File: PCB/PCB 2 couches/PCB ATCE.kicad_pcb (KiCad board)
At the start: 2 copper layers, 40.2 x 33.2 mm, 30 parts, among them J1 USB_OTG, J2 Conn_Coaxial, SW1 SW_Push, SW2 SW_Push, Y1 16MHz

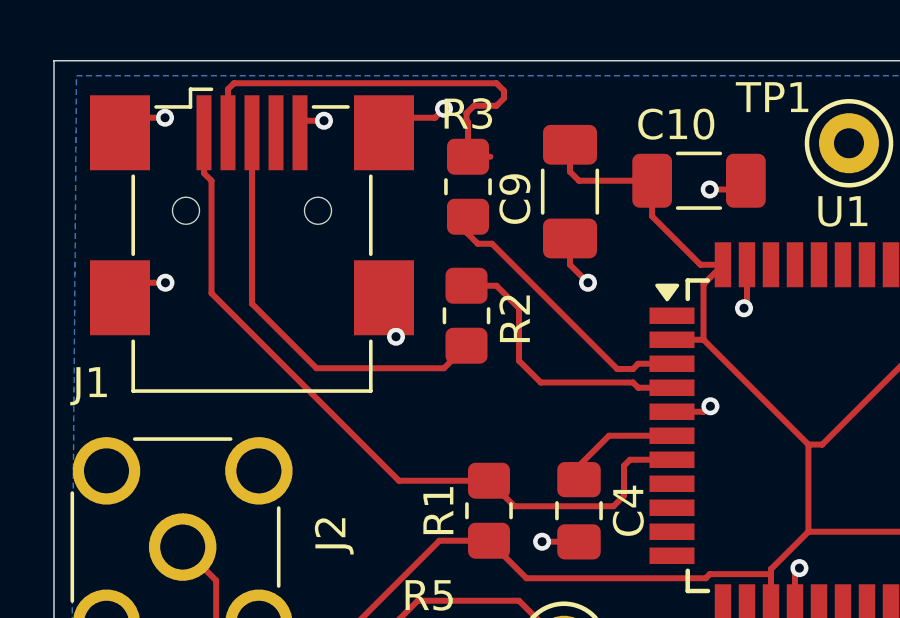
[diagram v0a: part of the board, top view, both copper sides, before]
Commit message: Modification du routage des paires différentielles de l'USB pour le PCB 2 couches
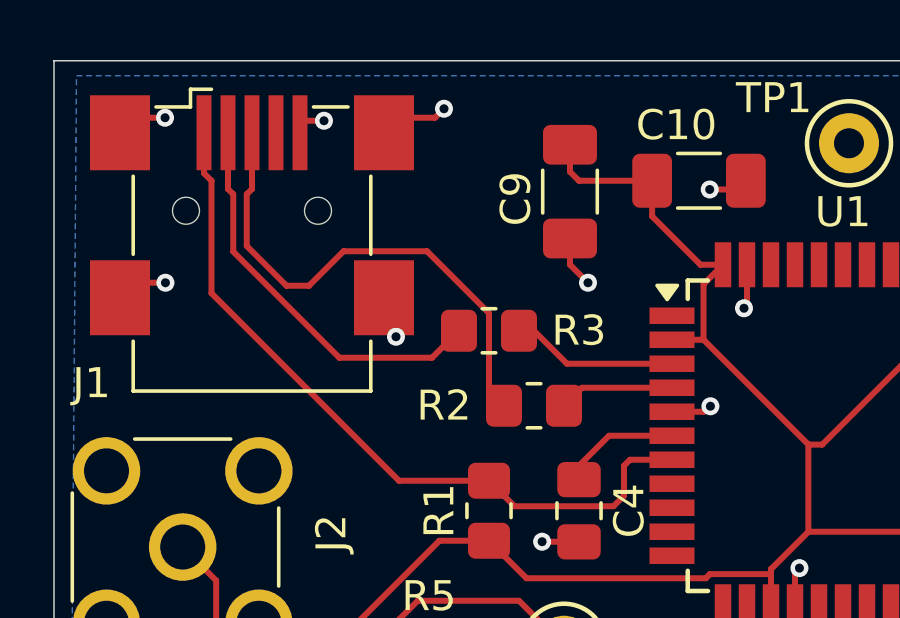
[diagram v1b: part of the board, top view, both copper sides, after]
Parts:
- moved R3 4.85 mm to (126.5, 86.0), turned to 0 degrees
- moved R2 3.75 mm to (128.0, 88.5), turned to 0 degrees
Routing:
- net /D2+: track 9.28 -> 3.85 mm
- net /D1+: track 14.1 -> 18.5 mm
- net /D2-: track 10.1 -> 5.78 mm

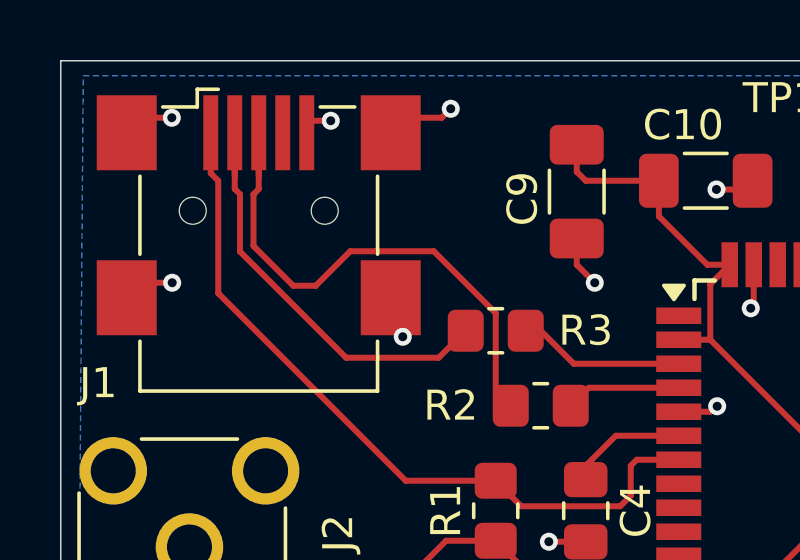
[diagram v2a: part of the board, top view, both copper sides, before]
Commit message: Changement des ports pour le PWM et l'ICP
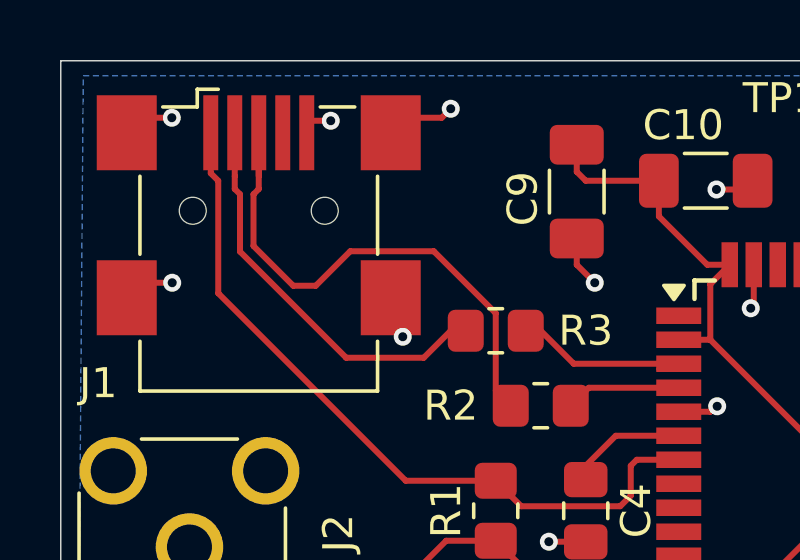
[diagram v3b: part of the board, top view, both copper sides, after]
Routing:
- net /D1-: track 14.8 -> 13.4 mm
- net /D1+: track 18.5 -> 17.4 mm
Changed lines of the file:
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@@
 	)
 	(segment
-		(start 126.5 85.415256)
-		(end 126.5 88)
+		(start 118.6 81.275001)
+		(end 118.425 81.450001)
+		(width 0.2)
+		(layer "F.Cu")
+		(net 12)
+	)
+	(segment
+		(start 120.5 84.5)
+		(end 121.65 83.35)
+		(width 0.2)
+		(layer "F.Cu")
+		(net 12)
+	)
+	(segment
+		(start 118.6 79.4)
+		(end 118.6 80.85)
 		(width 0.2)
 		(layer "F.Cu")
@@
 	)
 	(segment
-		(start 118.425 81.450001)
-		(end 118.425 83.175)
+		(start 126.5 88)
+		(end 127 88.5)
 		(width 0.2)
 		(layer "F.Cu")
@@
 	)
 	(segment
-		(start 124.434744 83.35)
-		(end 126.5 85.415256)
+		(start 126.5 85.415256)
+		(end 126.5 88)
 		(width 0.2)
 		(layer "F.Cu")
@@
 	)
 	(segment
-		(start 118.6 79.4)
-		(end 118.6 80.85)
+		(start 118.6 80.5)
+		(end 118.6 81.275001)
 		(width 0.2)
 		(layer "F.Cu")
@@
 	)
 	(segment
-		(start 118.6 81.275001)
-		(end 118.425 81.450001)
+		(start 124.434744 83.35)
+		(end 126.5 85.415256)
 		(width 0.2)
 		(layer "F.Cu")
@@
 	)
 	(segment
-		(start 120.5 84.5)
-		(end 121.65 83.35)
+		(start 118.425 81.450001)
+		(end 118.425 83.175)
 		(width 0.2)
 		(layer "F.Cu")
@@
 	)
 	(segment
-		(start 126.5 88)
-		(end 127 88.5)
-		(width 0.2)
-		(layer "F.Cu")
-		(net 12)
-	)
-	(segment
-		(start 118.6 79.4)
-		(end 118.6 81.275001)
-		(width 0.2)
-		(layer "F.Cu")
-		(net 12)
-	)
-	(segment
-		(start 117.975 81.450001)
-		(end 117.975 83.361368)
+		(start 117.8 80.85)
+		(end 117.8 81.275001)
 		(width 0.2)
 		(layer "F.Cu")
@@
 	)
 	(segment
-		(start 117.8 79.4)
-		(end 117.8 81.275001)
+		(start 124.10002 86.89998)
+		(end 125 86)
 		(width 0.2)
 		(layer "F.Cu")
@@
 	)
 	(segment
-		(start 117.8 79.4)
-		(end 117.8 80.85)
+		(start 121.513612 86.89998)
+		(end 124.10002 86.89998)
 		(width 0.2)
 		(layer "F.Cu")
@@
 	)
 	(segment
-		(start 121.513612 86.89998)
-		(end 124.60002 86.89998)
+		(start 117.8 79.4)
+		(end 117.8 80.85)
 		(width 0.2)
 		(layer "F.Cu")
@@
 	)
 	(segment
-		(start 124.60002 86.89998)
+		(start 125 86)
 		(end 125.5 86)
 		(width 0.2)
 		(layer "F.Cu")
+		(net 13)
+	)
+	(segment
+		(start 117.975 81.450001)
+		(end 117.975 83.361368)
+		(width 0.2)
+		(layer "F.Cu")

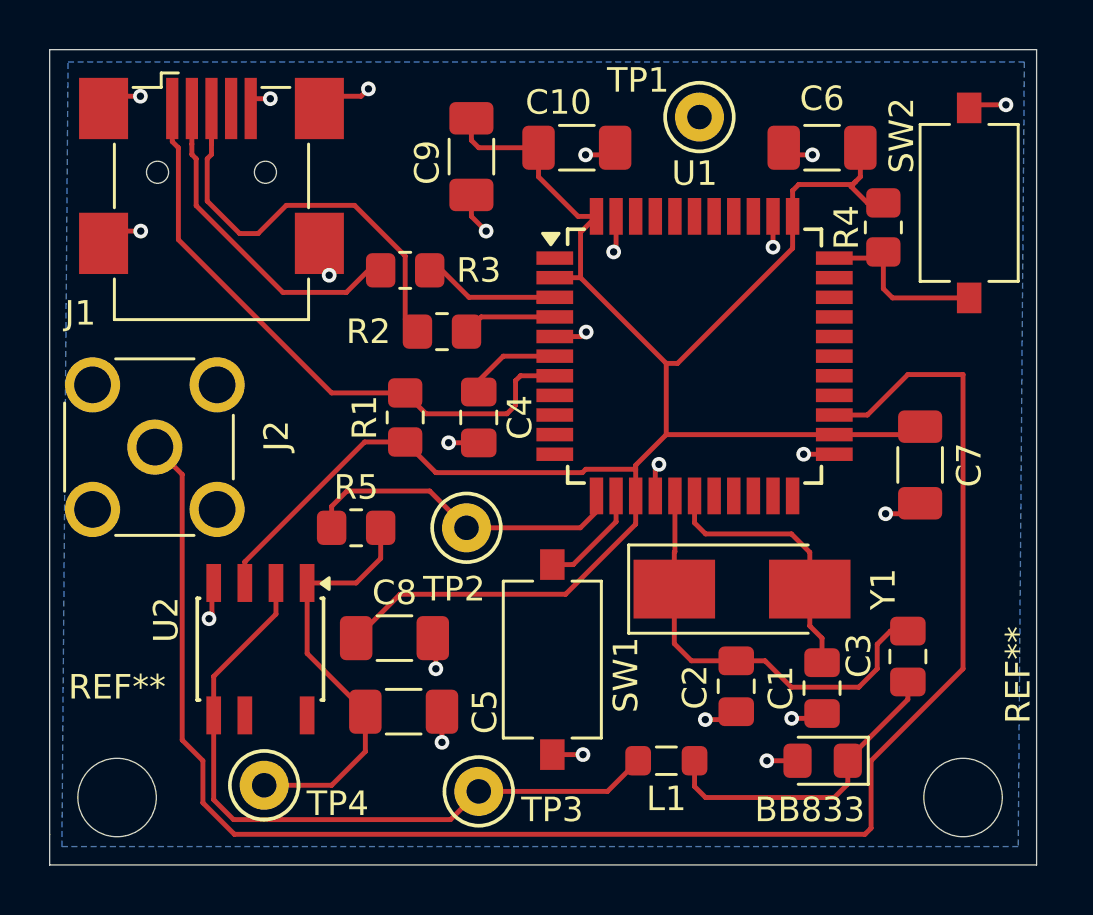
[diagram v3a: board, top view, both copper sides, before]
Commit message: modification pcb (empreinte test point + routage nouveau pwm)
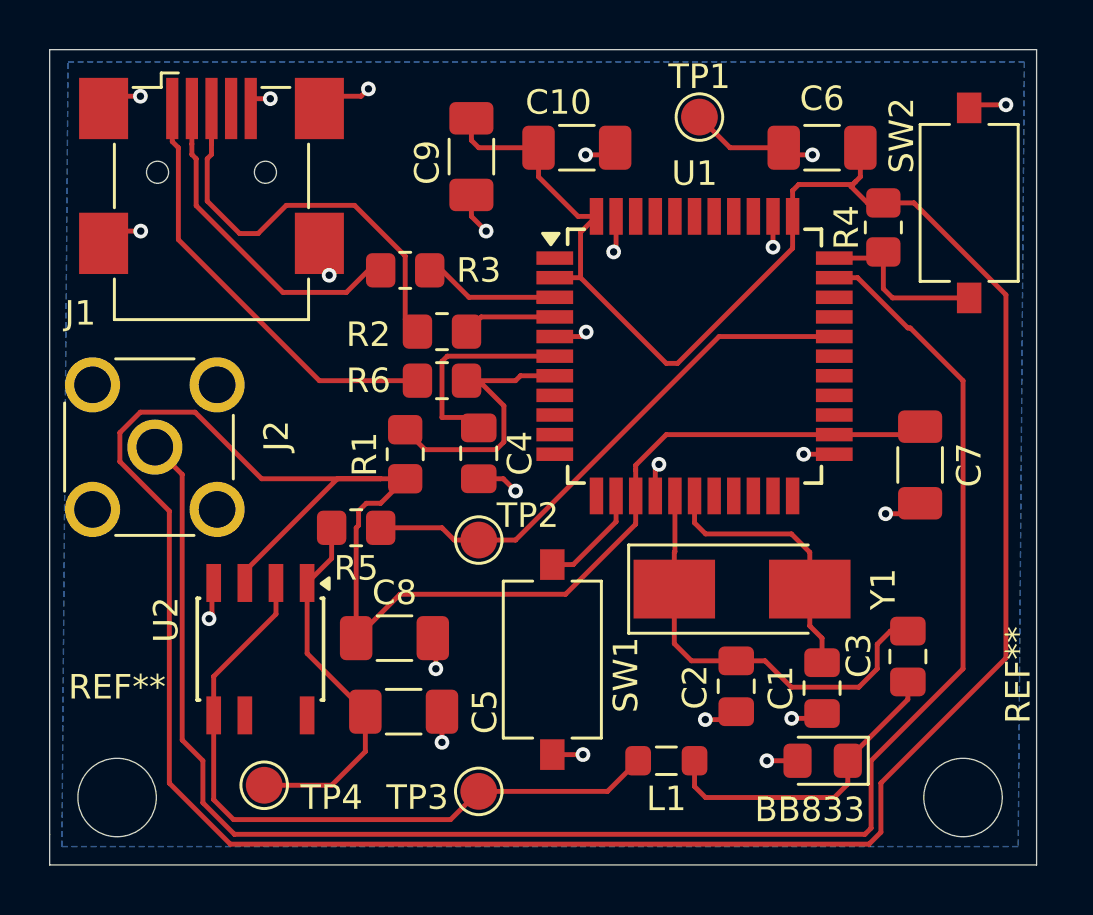
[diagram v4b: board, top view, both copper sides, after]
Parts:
- added R6: 0, Resistor_SMD:R_0805_2012Metric_Pad1.20x1.40mm_HandSolder, F.Cu at (128.0, 90.5)
- TP1, TP2, TP3, TP4: footprint TestPoint:TestPoint_Keystone_5000-5004_Miniature -> TestPoint:TestPoint_Pad_D1.5mm
- moved R1 1.50 mm to (126.5, 93.5)
- moved C4 1.46 mm to (129.5, 93.5)
- moved TP2 0.71 mm to (129.5, 97.0)
- turned R5 to 180 degrees
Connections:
- J1 pad 2: /D1- -> /D-
- J1 pad 3: /D1+ -> /D+
- R1 pad 2: Net-(J1-VBUS) -> Net-(U1-VBUS)
- R2 pad 1: /D1+ -> /D+
- R2 pad 2: /D2+ -> /D1+
- R3 pad 1: /D1- -> /D-
- R3 pad 2: /D2- -> /D1-
- R5 pad 1: Net-(U1-(OC0A/OC1C/~{RTS}/PCINT7)PB7) -> Net-(U1-(ADC12/OC1A/~{OC4B}/PCINT5)PB5)
- TP2 pad 1: Net-(U1-(OC0A/OC1C/~{RTS}/PCINT7)PB7) -> Net-(U1-(ADC12/OC1A/~{OC4B}/PCINT5)PB5)
- U1 pad 12: Net-(U1-(OC0A/OC1C/~{RTS}/PCINT7)PB7) -> unconnected-(U1-(OC0A/OC1C/~{RTS}/PCINT7)PB7-Pad12)
- U1 pad 25: Net-(J2-In) -> unconnected-(U1-(ICP1/ADC8)PD4-Pad25)
- U1 pad 29: unconnected-(U1-(ADC12/OC1A/~{OC4B}/PCINT5)PB5-Pad29) -> Net-(U1-(ADC12/OC1A/~{OC4B}/PCINT5)PB5)
- U1 pad 3: /D2- -> /D1-
- U1 pad 32: unconnected-(U1-(ICP3/CLK0/OC4A)PC7-Pad32) -> Net-(J2-In)
- U1 pad 4: /D2+ -> /D1+
- U1 pad 7: Net-(J1-VBUS) -> Net-(U1-VBUS)
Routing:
- net +5V: track 83.8 -> 165.8 mm
- net Net-(U1-(ADC12/OC1A/~{OC4B}/PCINT5)PB5): track 0.00 -> 22.1 mm
- net /D+: track 0.00 -> 17.4 mm
- net /D1+: track 17.4 -> 3.85 mm
- net Net-(U1-(OC0A/OC1C/~{RTS}/PCINT7)PB7): track 13.5 -> 0.00 mm
- net /D-: track 0.00 -> 13.4 mm
- net Net-(U1-VBUS): track 0.00 -> 12.1 mm
- net /D1-: track 13.4 -> 5.78 mm
- net Net-(J1-VBUS): track 25.5 -> 18.1 mm
- net /D2-: track 5.78 -> 0.00 mm
- net Net-(U1-UCAP): track 3.98 -> 8.65 mm
- net GND: track 32.5 -> 36.9 mm
- net /D2+: track 3.85 -> 0.00 mm
- net Net-(U2-+): track 17.7 -> 15.7 mm
- net Net-(J2-In): track 69.2 -> 70.0 mm

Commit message: pcb modif
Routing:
- net +5V: track 165.8 -> 164.0 mm

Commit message: prise des captures d'ecrans
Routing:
- net +5V: track 164.0 -> 161.0 mm
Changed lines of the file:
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@@
 		(tags "SMA THT Female Jack Horizontal")
 		(property "Reference" "J2"
-			(at 0.46 4.96 90)
+			(at 1.03 4.23 90)
 			(layer "F.SilkS")
 			(effects
@@
 	)
 	(segment
+		(start 126.5 94.5)
+		(end 122 94.5)
+		(width 0.2)
+		(layer "F.Cu")
+		(net 7)
+	)
+	(segment
 		(start 122 95)
 		(end 119.96 97.04)
@@
 	)
 	(segment
-		(start 122 94.5)
-		(end 125.5 94.5)
-		(width 0.2)
-		(layer "F.Cu")
-		(net 7)
-	)
-	(segment
 		(start 133.8517 86.5)
 		(end 133.6517 86.3)
@@
 	)
 	(segment
-		(start 125.5 94.5)
-		(end 122.5 94.5)
-		(width 0.2)
-		(layer "F.Cu")
-		(net 7)
-	)
-	(segment
 		(start 124.599 95.81484)
 		(end 124.599 96.401)
@@
 		(width 0.2)
 		(layer "F.Cu")
-		(net 7)
-	)
-	(segment
-		(start 126.5 94.5)
-		(end 125.5 94.5)
-		(width 0.2)
-		(layer "F.Cu")
